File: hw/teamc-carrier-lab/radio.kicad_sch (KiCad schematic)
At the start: 9 parts, among them J30 SP4 breakout

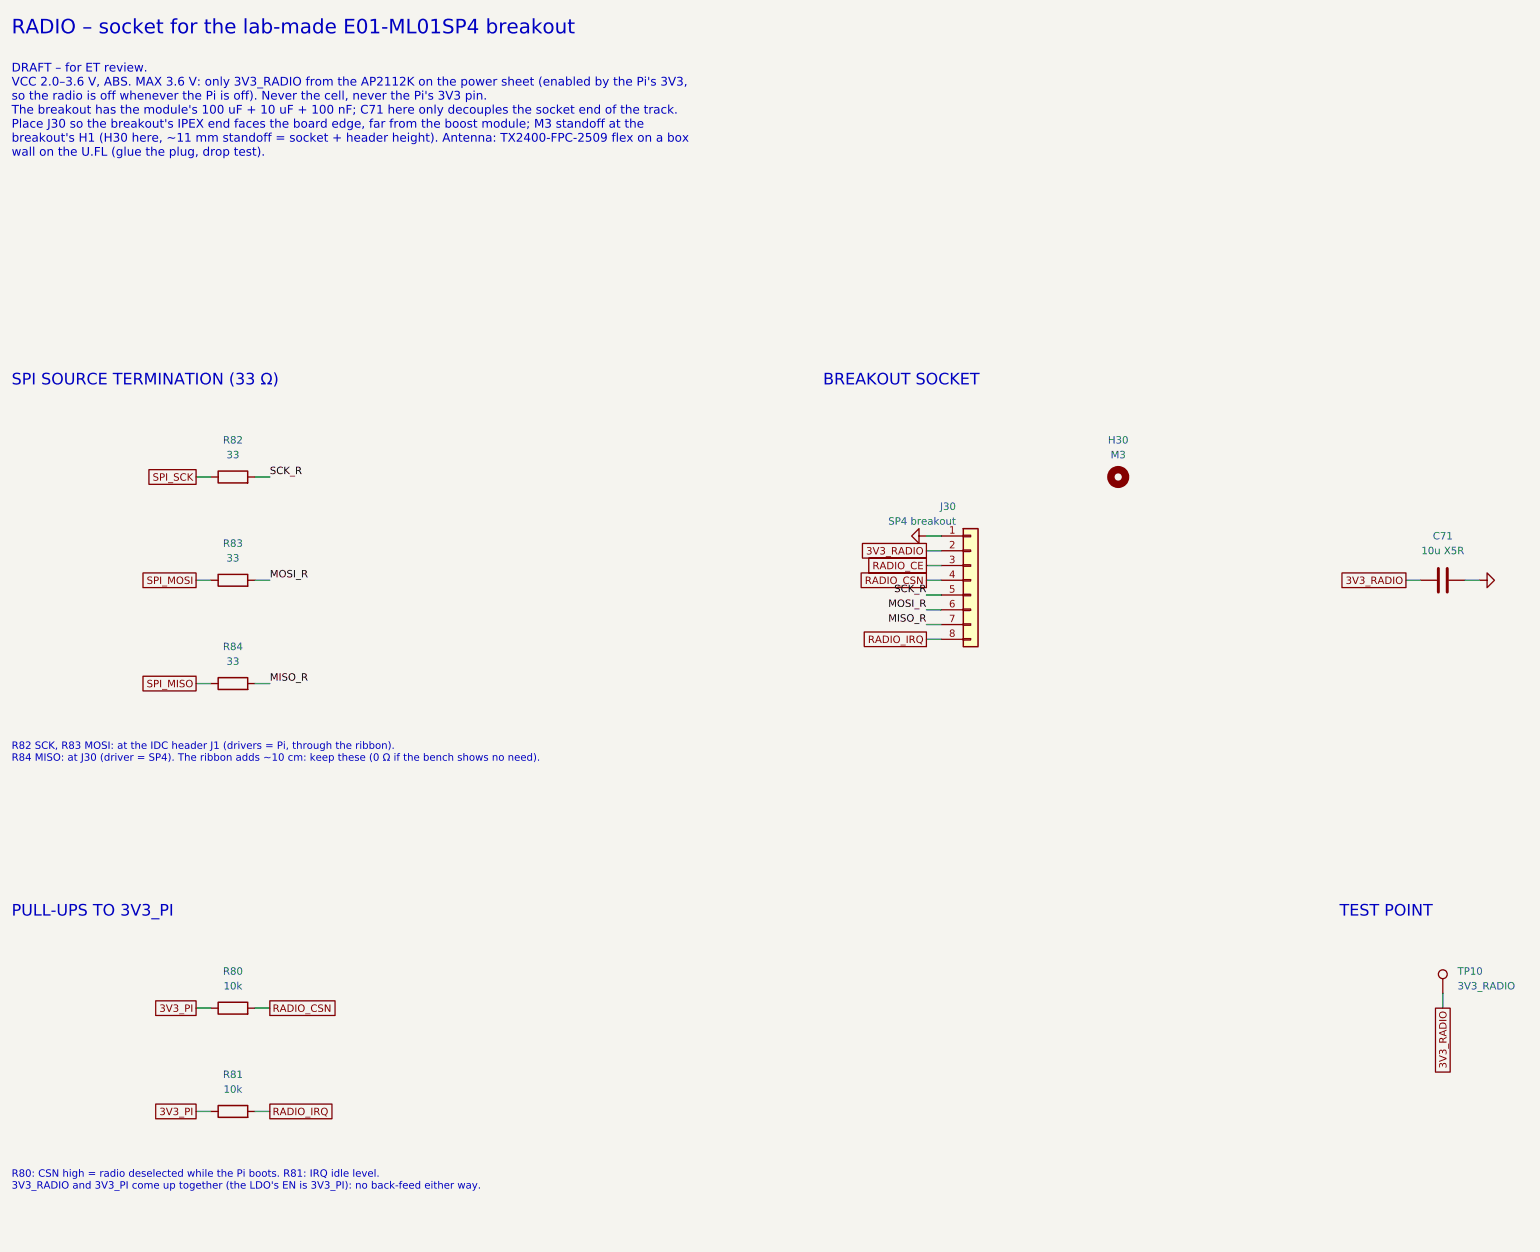
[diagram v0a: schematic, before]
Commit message: Carrier rev B (UPC lab): placed and routed on one copper layer, DRC 0/0/0
- place_carrier_lab.py: fixed floorplan (power right, J1 centre, SP4 socket top-left
  edge, UI leads left edge, fuel gauge bottom-left); provisional 100 x 80 mm outline
  until the box is measured.
- linkroute.py: single-layer grid router whose second "layer" is straight wire links
  (bare wire on the component side between two unplated holes).
- route_carrier_lab.py: hand-coded power path, SCK swap under R84/R83, left half; the
  rest routed in a topology order, --search over the band-net orders.
- finish_carrier_lab.py: GND pour (0.4 mm), FR10 no-fill areas, M3 keep-outs, ground
  island joins, links -> W parts (one-pin symbol, WireLink footprint with jumper pads).
- fab_carrier_lab.py: F.Cu + Edge.Cuts gerbers, drill, 1:1 copper PDFs, assembly and
  schematic PDFs, zip; renders; build_bom.py --rev b -> hw/BOM_revB.csv (~EUR 139).
- Schematic changes for one layer (documented on the sheets and in DESIGN_NOTES):
  1206 R/C, no UI pull-ups, 4 x SMF5.0A instead of SP0504, R80 to 3V3_RADIO, no R81,
  no C71/TP10/TP2 (C12 10 uF), 3V3_PI from J1 pin 1, FG_ALRT not routed, LED return
  on pin 25, J1 GND pins 20/30/34/39 unused, J23 on BAT_IN.
- ERC 0; DRC 0 violations / 0 unconnected / 0 parity (silk/mask checks off: the lab
  board has neither); 10 wire links (138 mm).

Co-Authored-By: Claude Opus 5.5 <noreply@anthropic.com>
Claude-Session: https://claude.ai/code/session_01M3xdFsssmBw3o2iBWKaKwo
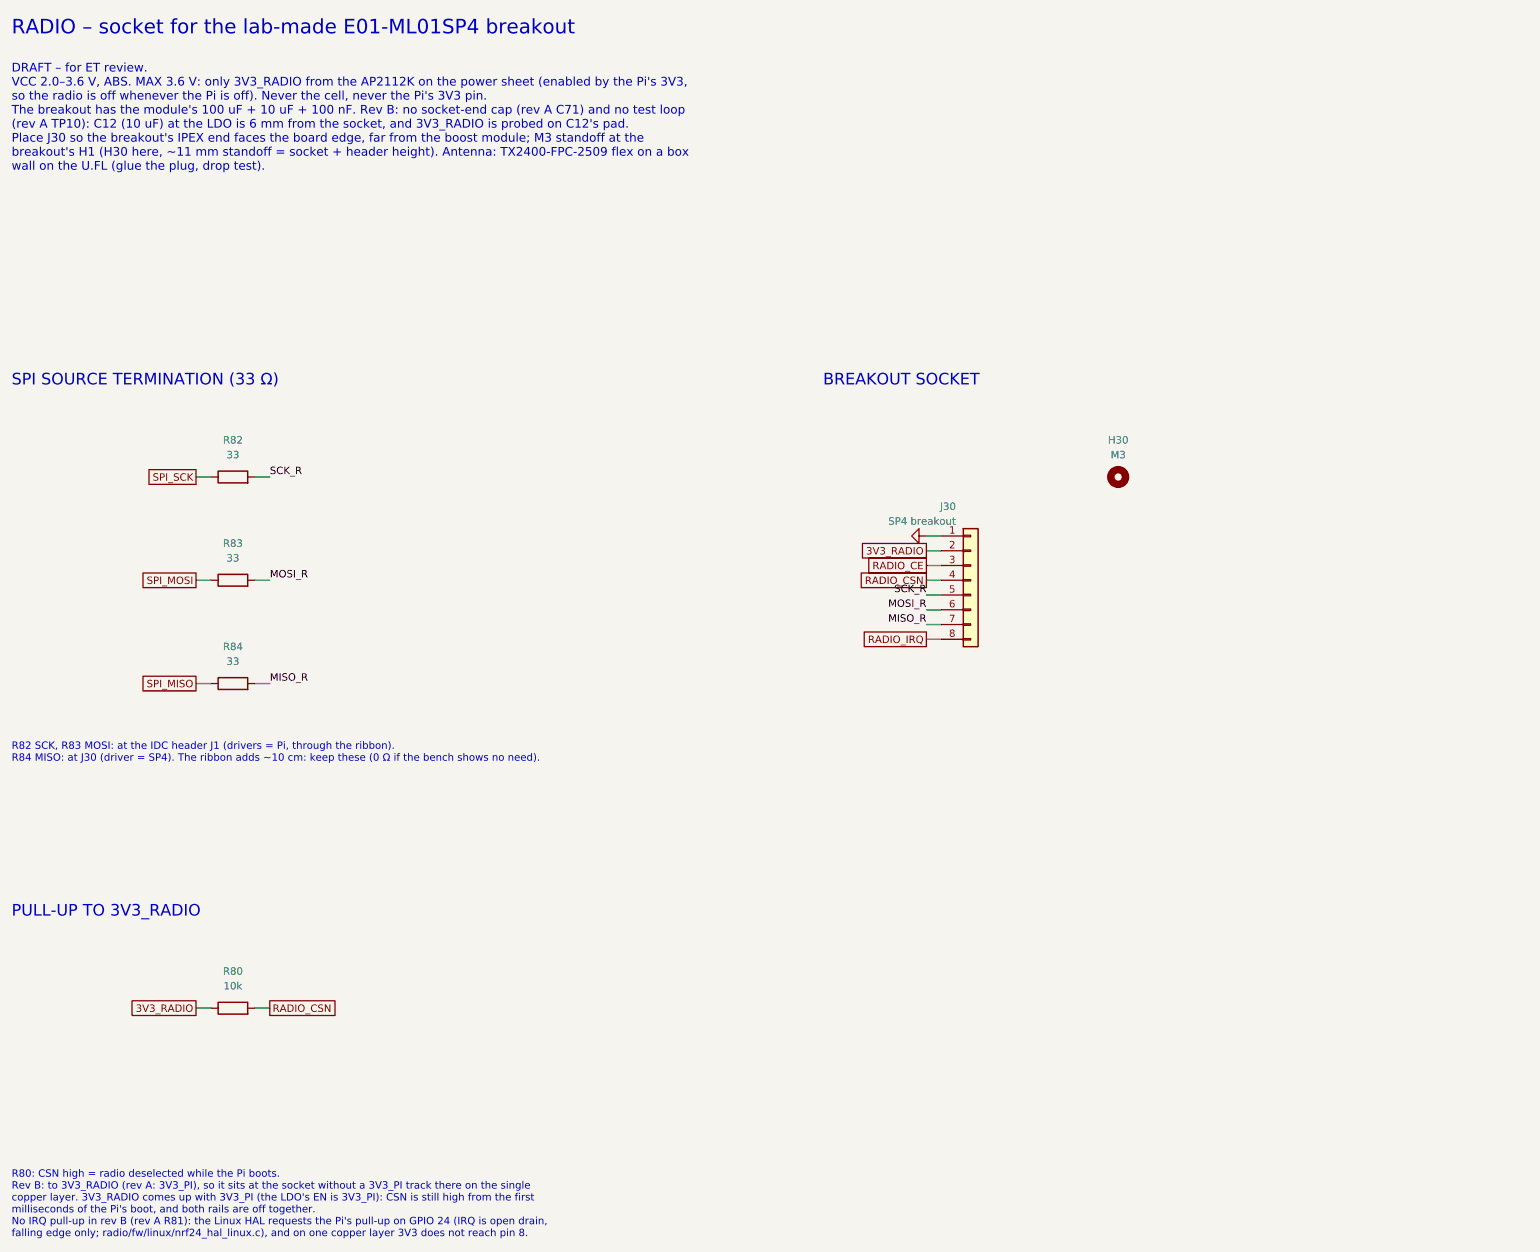
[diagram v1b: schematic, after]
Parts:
- removed C71: 10u X5R, Capacitor_SMD:C_0805_2012Metric_Pad1.18x1.45mm_HandSolder, symbol Device:C
- removed R81: 10k, Resistor_SMD:R_0805_2012Metric_Pad1.20x1.40mm_HandSolder, symbol Device:R
- removed TP10: 3V3_RADIO, TestPoint:TestPoint_Loop_D2.50mm_Drill1.0mm, symbol Connector:TestPoint
- R80: footprint Resistor_SMD:R_0805_2012Metric_Pad1.20x1.40mm_HandSolder -> Resistor_SMD:R_1206_3216Metric_Pad1.30x1.75mm_HandSolder; MPN RC0805FR-0710KL -> RC1206FR-0710KL
- R82, R83, R84: footprint Resistor_SMD:R_0805_2012Metric_Pad1.20x1.40mm_HandSolder -> Resistor_SMD:R_1206_3216Metric_Pad1.30x1.75mm_HandSolder; MPN RC0805FR-0733RL -> RC1206FR-0733RL
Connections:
- net 3V3_PI is gone; now on net 3V3_RADIO: R80.1
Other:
- note added: "DRAFT – for ET review. VCC 2.0–3.6 V, ABS. MAX 3.6 V: only 3V3_RADIO from the AP2112K on the power sheet (enabled by the Pi's 3V3, so the radio is off whenever the Pi is off). Never the cell, never the Pi's 3V3 pin. The breakout has the module's 100 uF + 10 uF + 100 nF. Rev B: no socket-end cap (rev A C71) and no test loop (rev A TP10): C12 (10 uF) at the LDO is 6 mm from the socket, and 3V3_RADI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"
- note added: "PULL-UP TO 3V3_RADIO"
- note added: "R80: CSN high = radio deselected while the Pi boots. Rev B: to 3V3_RADIO (rev A: 3V3_PI), so it sits at the socket without a 3V3_PI track there on the single copper layer. 3V3_RADIO comes up with 3V3_PI (the LDO's EN is 3V3_PI): CSN is still high from the first milliseconds of the Pi's boot, and both rails are off together. No IRQ pull-up in rev B (rev A R81): the Linux HAL requests the Pi's pull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"
- note removed: "DRAFT – for ET review. VCC 2.0–3.6 V, ABS. MAX 3.6 V: only 3V3_RADIO from the AP2112K on the power sheet (enabled by the Pi's 3V3, so the radio is off whenever the Pi is off). Never the cell, never the Pi's 3V3 pin. The breakout has the module's 100 uF + 10 uF + 100 nF; C71 here only decouples the socket end of the track. Place J30 so the breakout's IPEX end faces the board edge, far from the boo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"
- note removed: "PULL-UPS TO 3V3_PI"
- note removed: "R80: CSN high = radio deselected while the Pi boots. R81: IRQ idle level. 3V3_RADIO and 3V3_PI come up together (the LDO's EN is 3V3_PI): no back-feed either way."
- note removed: "TEST POINT"
